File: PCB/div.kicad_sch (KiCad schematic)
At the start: 29 parts, among them J2 Bus Gate Reset, Q4 BC557, U1 4024

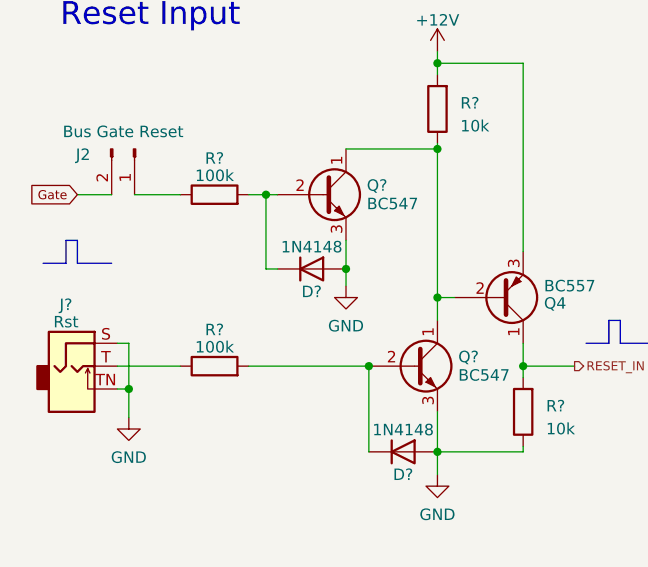
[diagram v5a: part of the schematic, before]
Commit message: :art: Add a pull-down resistor to open bus gate reset
If the jumper is not set, the bus gate reset would be floating. Add a
(very large) pull-down resistor to keep this at GND.
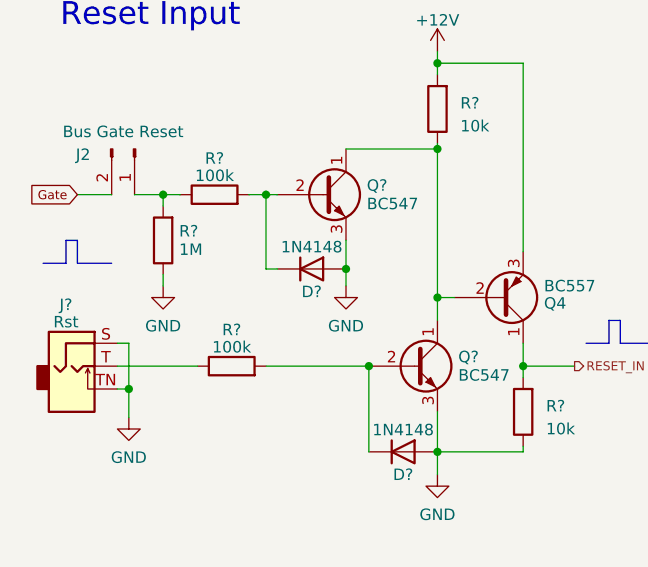
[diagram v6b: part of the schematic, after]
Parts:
- added R?: 1M, Resistor_THT:R_Axial_DIN0207_L6.3mm_D2.5mm_P7.62mm_Horizontal, symbol Device:R
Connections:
- net GND: now also R?.1
- net at J2.1 (Pin_1), R?.1: now also R?.2
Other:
- moved on the sheet: R?
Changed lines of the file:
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@@
   (junction (at 61.595 133.35) (diameter 0) (color 0 0 0 0)
+  )
+  (junction (at 31.115 104.775) (diameter 0) (color 0 0 0 0)
   )
   (junction (at 103.505 27.94) (diameter 0) (color 0 0 0 0)
@@
     (stroke (width 0) (type default))
   )
+  (wire (pts (xy 31.115 113.665) (xy 31.115 114.935))
+    (stroke (width 0) (type default))
+  )
   (polyline (pts (xy 81.915 118.745) (xy 81.915 121.285))
     (stroke (width 0) (type solid))
@@
     (stroke (width 0) (type default))
   )
-  (wire (pts (xy 27.94 104.775) (xy 33.02 104.775))
+  (wire (pts (xy 27.94 104.775) (xy 31.115 104.775))
     (stroke (width 0) (type default))
   )
@@
     (stroke (width 0) (type default))
   )
+  (wire (pts (xy 31.115 106.045) (xy 31.115 104.775))
+    (stroke (width 0) (type default))
+  )
   (wire (pts (xy 113.03 97.155) (xy 102.87 97.155))
     (stroke (width 0) (type default))
@@
     (stroke (width 0) (type solid))
   )
+  (wire (pts (xy 31.115 104.775) (xy 33.02 104.775))
+    (stroke (width 0) (type default))
+  )
   (wire (pts (xy 91.44 186.69) (xy 109.22 186.69))
     (stroke (width 0) (type default))
@@
     (stroke (width 0) (type default))
   )
-  (wire (pts (xy 26.035 123.825) (xy 33.02 123.825))
+  (wire (pts (xy 26.035 123.825) (xy 34.925 123.825))
     (stroke (width 0) (type default))
   )
@@
     (stroke (width 0) (type solid))
   )
-  (wire (pts (xy 40.64 123.825) (xy 53.975 123.825))
+  (wire (pts (xy 42.545 123.825) (xy 53.975 123.825))
     (stroke (width 0) (type default))
   )
@@
         (path "/69636855-5bea-4b1f-bae0-d5724c7c5e69"
           (reference "Q4") (unit 1)
+        )
+      )
+    )
+  )
+  (symbol (lib_id "power:GND") (at 31.115 114.935 0) (unit 1)
+    (in_bom yes) (on_board yes) (dnp no) (fields_autoplaced)
+    (property "Reference" "#PWR?" (at 31.115 121.285 0)
+      (effects (font (size 1.27 1.27)) hide)
+    )
+    (property "Value" "GND" (at 31.115 119.3784 0)
+      (effects (font (size 1.27 1.27)))
+    )
+    (property "Footprint" "" (at 31.115 114.935 0)
+      (effects (font (size 1.27 1.27)) hide)
+    )
+    (property "Datasheet" "" (at 31.115 114.935 0)
+      (effects (font (size 1.27 1.27)) hide)
+    )
+    (pin "1")
+    (instances
+      (project "manual-gate-trigger-source"
+        (path "/64d6412c-bfad-42df-9ed7-bcc6cbff0470/fd0933f7-8da4-4985-a361-ff361c3b6a05"
+          (reference "#PWR?") (unit 1)
+        )
+      )
+      (project "div"
+        (path "/69636855-5bea-4b1f-bae0-d5724c7c5e69"
+          (reference "#PWR041") (unit 1)
         )
       )
@@
     )
   )
+  (symbol (lib_id "Device:R") (at 31.115 109.855 180) (unit 1)
+    (in_bom yes) (on_board yes) (dnp no) (fields_autoplaced)
+    (property "Reference" "R?" (at 32.893 108.831 0)
+      (effects (font (size 1.27 1.27)) (justify right))
+    )
+    (property "Value" "1M" (at 32.893 110.879 0)
+      (effects (font (size 1.27 1.27)) (justify right))
+    )
+    (property "Footprint" "Resistor_THT:R_Axial_DIN0207_L6.3mm_D2.5mm_P7.62mm_Horizontal" (at 32.893 109.855 90)
+      (effects (font (size 1.27 1.27)) hide)
+    )
+    (property "Datasheet" "~" (at 31.115 109.855 0)
+      (effects (font (size 1.27 1.27)) hide)
+    )
+    (pin "1")
+    (pin "2")
+    (instances
+      (project "manual-gate-trigger-source"
+        (path "/64d6412c-bfad-42df-9ed7-bcc6cbff0470/fd0933f7-8da4-4985-a361-ff361c3b6a05"
+          (reference "R?") (unit 1)
+        )
+      )
+      (project "div"
+        (path "/69636855-5bea-4b1f-bae0-d5724c7c5e69"
+          (reference "R27") (unit 1)
+        )
+      )
+    )
+  )
   (symbol (lib_id "Device:LED") (at 113.03 91.44 90) (unit 1)
     (in_bom no) (on_board yes) (dnp yes)
@@
     )
   )
-  (symbol (lib_id "Device:R") (at 36.83 123.825 90) (unit 1)
-    (in_bom yes) (on_board yes) (dnp no) (fields_autoplaced)
-    (property "Reference" "R?" (at 36.83 119.7991 90)
-      (effects (font (size 1.27 1.27)))
-    )
-    (property "Value" "100k" (at 36.83 121.7201 90)
-      (effects (font (size 1.27 1.27)))
-    )
-    (property "Footprint" "Resistor_THT:R_Axial_DIN0207_L6.3mm_D2.5mm_P7.62mm_Horizontal" (at 36.83 125.603 90)
-      (effects (font (size 1.27 1.27)) hide)
-    )
-    (property "Datasheet" "~" (at 36.83 123.825 0)
-      (effects (font (size 1.27 1.27)) hide)
-    )
+  (symbol (lib_id "Device:R") (at 38.735 123.825 90) (unit 1)
+    (in_bom yes) (on_board yes) (dnp no) (fields_autoplaced)
+    (property "Reference" "R?" (at 38.735 119.7991 90)
+      (effects (font (size 1.27 1.27)))
+    )
+    (property "Value" "100k" (at 38.735 121.7201 90)
+      (effects (font (size 1.27 1.27)))
+    )
+    (property "Footprint" "Resistor_THT:R_Axial_DIN0207_L6.3mm_D2.5mm_P7.62mm_Horizontal" (at 38.735 125.603 90)
+      (effects (font (size 1.27 1.27)) hide)
+    )
+    (property "Datasheet" "~" (at 38.735 123.825 0)
+      (effects (font (size 1.27 1.27)) hide)
+    )

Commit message: :art: Add a pull-down resistor to the reset input
Attaching a cable and touching the other end triggers the reset.
Add a (very large) pull-down resistor to prevent the line from
floating.
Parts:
- added R?: 1M, Resistor_THT:R_Axial_DIN0207_L6.3mm_D2.5mm_P7.62mm_Horizontal, symbol Device:R
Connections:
- net GND: now also R?.1
- net at J?.T, R?.1: now also R?.2
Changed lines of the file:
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@@
   (junction (at 33.02 171.45) (diameter 0) (color 0 0 0 0)
   )
+  (junction (at 31.75 123.825) (diameter 0) (color 0 0 0 0)
+  )
   (junction (at 61.595 90.17) (diameter 0) (color 0 0 0 0)
   )
@@
   )
   (junction (at 51.435 46.355) (diameter 0) (color 0 0 0 0)
+  )
+  (junction (at 27.305 133.985) (diameter 0) (color 0 0 0 0)
   )
   (no_connect (at 45.72 173.99))
@@
     (stroke (width 0) (type default))
   )
+  (wire (pts (xy 31.75 123.825) (xy 34.925 123.825))
+    (stroke (width 0) (type default))
+  )
   (wire (pts (xy 179.705 95.25) (xy 197.485 95.25))
     (stroke (width 0) (type default))
@@
     (stroke (width 0) (type default))
   )
+  (wire (pts (xy 27.305 133.985) (xy 31.75 133.985))
+    (stroke (width 0) (type default))
+  )
   (wire (pts (xy 61.595 128.905) (xy 61.595 133.35))
     (stroke (width 0) (type default))
@@
     (stroke (width 0) (type default))
   )
+  (wire (pts (xy 31.75 132.715) (xy 31.75 133.985))
+    (stroke (width 0) (type default))
+  )
   (wire (pts (xy 113.03 95.25) (xy 113.03 97.155))
     (stroke (width 0) (type default))
@@
     (stroke (width 0) (type solid))
   )
+  (wire (pts (xy 27.305 133.985) (xy 27.305 135.255))
+    (stroke (width 0) (type default))
+  )
   (wire (pts (xy 31.115 104.775) (xy 33.02 104.775))
     (stroke (width 0) (type default))
@@
     (stroke (width 0) (type default))
   )
-  (wire (pts (xy 26.035 123.825) (xy 34.925 123.825))
+  (wire (pts (xy 26.035 123.825) (xy 31.75 123.825))
     (stroke (width 0) (type default))
   )
@@
     (stroke (width 0) (type default))
   )
+  (wire (pts (xy 31.75 125.095) (xy 31.75 123.825))
+    (stroke (width 0) (type default))
+  )
   (polyline (pts (xy 67.31 173.99) (xy 67.31 196.85))
     (stroke (width 0) (type default))
@@
     (stroke (width 0) (type default))
   )
-  (wire (pts (xy 27.305 126.365) (xy 27.305 129.54))
+  (wire (pts (xy 27.305 126.365) (xy 27.305 133.985))
     (stroke (width 0) (type default))
   )
@@
   (hierarchical_label "CLOCK_IN" (shape output) (at 66.04 38.735 0) (fields_autoplaced)
     (effects (font (size 1 1)) (justify left))
+  )
+  (symbol (lib_id "Device:R") (at 31.75 128.905 180) (unit 1)
+    (in_bom yes) (on_board yes) (dnp no) (fields_autoplaced)
+    (property "Reference" "R?" (at 33.528 127.881 0)
+      (effects (font (size 1.27 1.27)) (justify right))
+    )
+    (property "Value" "1M" (at 33.528 129.929 0)
+      (effects (font (size 1.27 1.27)) (justify right))
+    )
+    (property "Footprint" "Resistor_THT:R_Axial_DIN0207_L6.3mm_D2.5mm_P7.62mm_Horizontal" (at 33.528 128.905 90)
+      (effects (font (size 1.27 1.27)) hide)
+    )
+    (property "Datasheet" "~" (at 31.75 128.905 0)
+      (effects (font (size 1.27 1.27)) hide)
+    )
+    (pin "1")
+    (pin "2")
+    (instances
+      (project "manual-gate-trigger-source"
+        (path "/64d6412c-bfad-42df-9ed7-bcc6cbff0470/fd0933f7-8da4-4985-a361-ff361c3b6a05"
+          (reference "R?") (unit 1)
+        )
+      )
+      (project "div"
+        (path "/69636855-5bea-4b1f-bae0-d5724c7c5e69"
+          (reference "R28") (unit 1)
+        )
+      )
+    )
   )
   (symbol (lib_name "GND_1") (lib_id "power:GND") (at 155.575 112.395 0) (unit 1)
@@
     )
   )
-  (symbol (lib_id "power:GND") (at 27.305 129.54 0) (unit 1)
-    (in_bom yes) (on_board yes) (dnp no) (fields_autoplaced)
-    (property "Reference" "#PWR?" (at 27.305 135.89 0)
-      (effects (font (size 1.27 1.27)) hide)
-    )
-    (property "Value" "GND" (at 27.305 133.9834 0)
-      (effects (font (size 1.27 1.27)))
-    )
-    (property "Footprint" "" (at 27.305 129.54 0)
-      (effects (font (size 1.27 1.27)) hide)
-    )
-    (property "Datasheet" "" (at 27.305 129.54 0)
-      (effects (font (size 1.27 1.27)) hide)
-    )
+  (symbol (lib_id "power:GND") (at 27.305 135.255 0) (unit 1)
+    (in_bom yes) (on_board yes) (dnp no) (fields_autoplaced)
+    (property "Reference" "#PWR?" (at 27.305 141.605 0)
+      (effects (font (size 1.27 1.27)) hide)
+    )
+    (property "Value" "GND" (at 27.305 139.6984 0)
+      (effects (font (size 1.27 1.27)))
+    )
+    (property "Footprint" "" (at 27.305 135.255 0)
+      (effects (font (size 1.27 1.27)) hide)
+    )
+    (property "Datasheet" "" (at 27.305 135.255 0)
+      (effects (font (size 1.27 1.27)) hide)
+    )

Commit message: :art: Add a pull-down resistor to the clock input
Keep this input from floating when only one end of the patch cable
is connected by adding a (very large) pull-down resistor.
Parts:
- added R?: 1M, Resistor_THT:R_Axial_DIN0207_L6.3mm_D2.5mm_P7.62mm_Horizontal, symbol Device:R
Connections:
- net GND: now also R?.1
- net at J?.T, R?.1: now also R?.2
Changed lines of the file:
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@@
   (junction (at 73.66 186.69) (diameter 0) (color 0 0 0 0)
   )
+  (junction (at 40.005 46.355) (diameter 0) (color 0 0 0 0)
+  )
   (junction (at 91.44 179.07) (diameter 0) (color 0 0 0 0)
   )
@@
   )
   (junction (at 31.115 104.775) (diameter 0) (color 0 0 0 0)
+  )
+  (junction (at 37.465 55.245) (diameter 0) (color 0 0 0 0)
   )
   (junction (at 103.505 27.94) (diameter 0) (color 0 0 0 0)
@@
     (stroke (width 0) (type default))
   )
+  (wire (pts (xy 37.465 55.245) (xy 37.465 56.515))
+    (stroke (width 0) (type default))
+  )
   (wire (pts (xy 37.465 43.815) (xy 37.465 48.895))
     (stroke (width 0) (type default))
@@
     (stroke (width 0) (type solid))
   )
+  (wire (pts (xy 40.005 55.245) (xy 37.465 55.245))
+    (stroke (width 0) (type default))
+  )
   (wire (pts (xy 51.435 46.355) (xy 51.435 53.975))
     (stroke (width 0) (type default))
@@
     (stroke (width 0) (type default))
   )
-  (wire (pts (xy 36.195 46.355) (xy 41.275 46.355))
+  (wire (pts (xy 36.195 46.355) (xy 40.005 46.355))
     (stroke (width 0) (type default))
   )
@@
     (stroke (width 0) (type default))
   )
+  (wire (pts (xy 40.005 46.355) (xy 41.275 46.355))
+    (stroke (width 0) (type default))
+  )
   (polyline (pts (xy 20.32 45.085) (xy 20.32 42.545))
     (stroke (width 0) (type solid))
@@
     (stroke (width 0) (type solid))
   )
+  (wire (pts (xy 40.005 54.61) (xy 40.005 55.245))
+    (stroke (width 0) (type default))
+  )
   (wire (pts (xy 71.12 132.715) (xy 71.12 133.35))
     (stroke (width 0) (type default))
@@
     (stroke (width 0) (type default))
   )
+  (wire (pts (xy 40.005 46.99) (xy 40.005 46.355))
+    (stroke (width 0) (type default))
+  )
   (wire (pts (xy 51.435 113.03) (xy 51.435 114.935))
     (stroke (width 0) (type default))
@@
     (stroke (width 0) (type default))
   )
-  (wire (pts (xy 37.465 48.895) (xy 37.465 56.515))
+  (wire (pts (xy 37.465 48.895) (xy 37.465 55.245))
     (stroke (width 0) (type default))
   )
@@
         )
       )
+    )
+  )
+  (symbol (lib_id "Device:R") (at 40.005 50.8 180) (unit 1)
+    (in_bom yes) (on_board yes) (dnp no) (fields_autoplaced)
+    (property "Reference" "R?" (at 41.783 49.776 0)
+      (effects (font (size 1.27 1.27)) (justify right))
+    )
+    (property "Value" "1M" (at 41.783 51.824 0)
+      (effects (font (size 1.27 1.27)) (justify right))
+    )
+    (property "Footprint" "Resistor_THT:R_Axial_DIN0207_L6.3mm_D2.5mm_P7.62mm_Horizontal" (at 41.783 50.8 90)
+      (effects (font (size 1.27 1.27)) hide)
+    )
+    (property "Datasheet" "~" (at 40.005 50.8 0)
+      (effects (font (size 1.27 1.27)) hide)
+    )
+    (pin "1")
+    (pin "2")
+    (instances
+      (project "manual-gate-trigger-source"
+        (path "/64d6412c-bfad-42df-9ed7-bcc6cbff0470/fd0933f7-8da4-4985-a361-ff361c3b6a05"
+          (reference "R?") (unit 1)
+        )
+      )
+      (project "div"
+        (path "/69636855-5bea-4b1f-bae0-d5724c7c5e69"
+          (reference "R29") (unit 1)
+        )
+      )
